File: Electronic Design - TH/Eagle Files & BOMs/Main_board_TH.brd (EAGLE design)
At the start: 90 x 137.2 mm, 41 parts, among them M1 ARDUINO-NANO-3.0, Q1 IRF9520, Q2 IRF9520

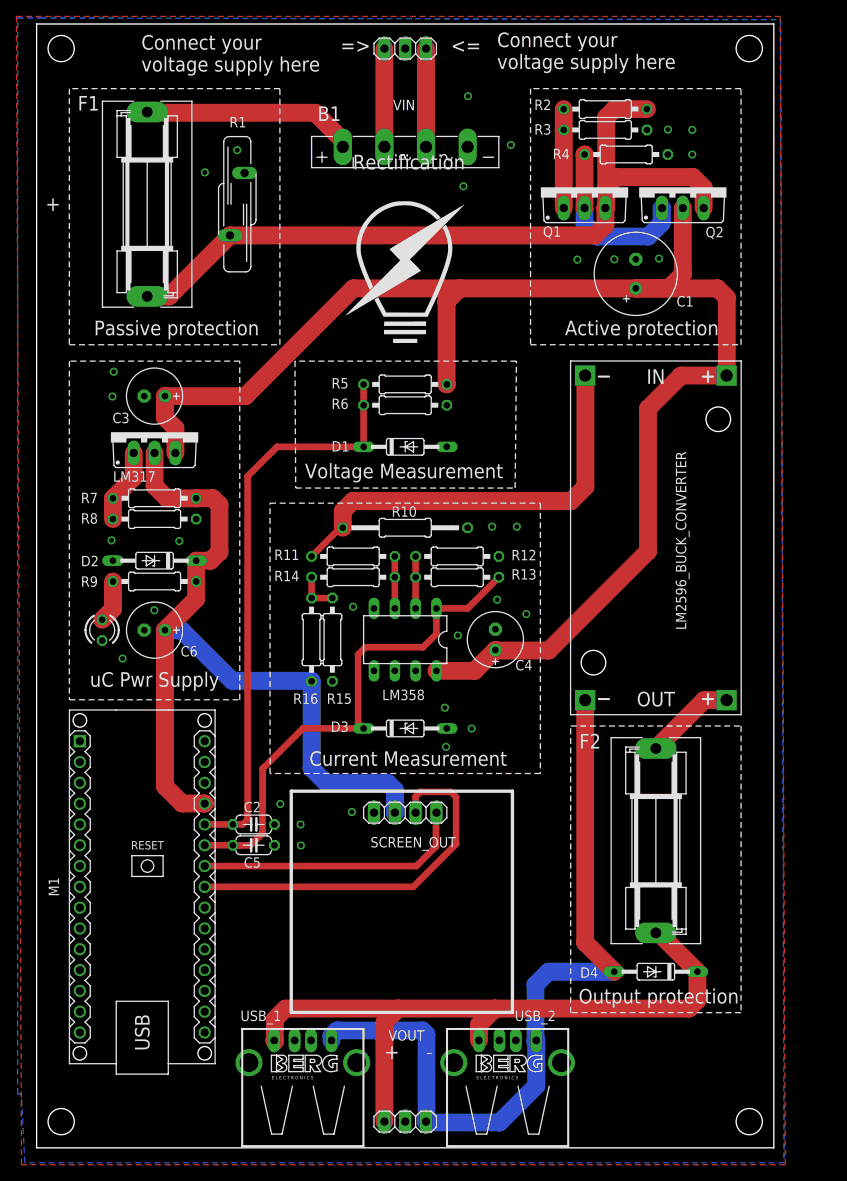
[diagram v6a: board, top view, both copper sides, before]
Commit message: Redoing names of sections so that they fit and adding in versioning and a place for people to put their names
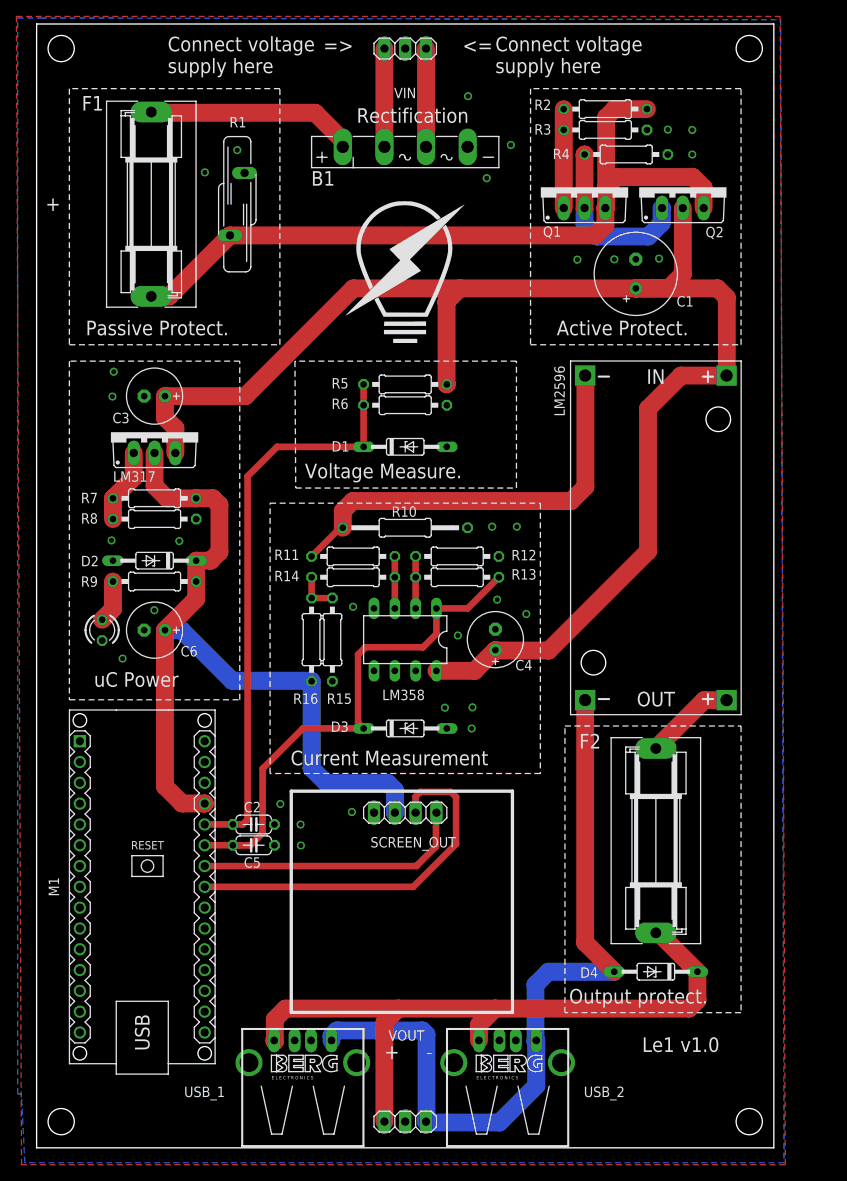
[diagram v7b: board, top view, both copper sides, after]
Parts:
- moved F1 0.50 mm to (14.0, 115.0)
- renumbered LM2596_BUCK_CONVERTER to LM2596
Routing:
- net VIN_UNPROTECTED: track 93.6 -> 93.1 mm
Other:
- board text added: "Active Protect."
- board text added: "Connect voltage supply here"
- board text added: "Le1 v1.0"
- board text added: "Output protect."
- board text added: "Passive Protect."
- board text added: "This Le1 belongs to:"
- board text added: "Voltage Measure."
- board text added: "uC Power"
- board text removed: "Active protection"
- board text removed: "Connect your voltage supply here"
- board text removed: "Output protection"
- board text removed: "Passive protection"
- board text removed: "Voltage Measurement"
- board text removed: "uC Pwr Supply"

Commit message: minor cosmetic changes in the silkscreen layer
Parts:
- moved D4 1.35 mm to (74.2, 21.3)
- moved F2 1.35 mm to (74.2, 37.3)
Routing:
- net VOUT_PREFUSE: track 11.1 -> 16.9 mm
- net VOUT_FINAL: track 85.1 -> 81.8 mm
- net N$10: track 96.1 -> 94.2 mm
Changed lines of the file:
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@@
 <wire x1="31.09" y1="16.34" x2="58.09" y2="16.34" width="0.4064" layer="21"/>
 <wire x1="58.09" y1="16.34" x2="58.09" y2="43.34" width="0.4064" layer="21"/>
-<text x="16" y="131" size="1.778" layer="25">Connect voltage
+<text x="34.5" y="135.5" size="1.778" layer="25" rot="R180">Connect voltage
 supply here </text>
 <wire x1="29.7" y1="129.11" x2="4" y2="129.11" width="0.15" layer="21" style="shortdash"/>
@@
 <wire x1="29.7" y1="97.84" x2="29.7" y2="129.11" width="0.15" layer="21" style="shortdash"/>
 <text x="52" y="133.5" size="1.778" layer="25">&lt;=</text>
-<text x="39.0672" y="124.9396" size="1.778" layer="25">Rectification</text>
-<text x="6" y="99" size="1.778" layer="25">Passive Protect.</text>
+<text x="37" y="124.9396" size="1.778" layer="25">Rectification</text>
+<text x="5.5" y="99" size="1.778" layer="25">Passive Protect.</text>
 <text x="63.5" y="99" size="1.778" layer="25">Active Protect.</text>
 <wire x1="61.5" y1="45.5" x2="28.5" y2="45.5" width="0.15" layer="21" style="shortdash"/>
@@
 <text x="32.75" y="81.54" size="1.778" layer="25">Voltage Measure.</text>
 <text x="31" y="46.5" size="1.778" layer="25">Current Measurement</text>
-<wire x1="86" y1="16.3" x2="64.5" y2="16.3" width="0.15" layer="21" style="shortdash"/>
-<wire x1="64.5" y1="16.3" x2="64.5" y2="51.3" width="0.15" layer="21" style="shortdash"/>
-<wire x1="64.5" y1="51.3" x2="86" y2="51.3" width="0.15" layer="21" style="shortdash"/>
+<wire x1="86" y1="16.3" x2="62.5" y2="16.3" width="0.15" layer="21" style="shortdash"/>
+<wire x1="62.5" y1="16.3" x2="62.5" y2="51.3" width="0.15" layer="21" style="shortdash"/>
+<wire x1="62.5" y1="51.3" x2="86" y2="51.3" width="0.15" layer="21" style="shortdash"/>
 <wire x1="86" y1="51.3" x2="86" y2="16.3" width="0.15" layer="21" style="shortdash"/>
-<text x="65" y="17.42" size="1.778" layer="25">Output protect.</text>
+<text x="64" y="17.42" size="1.778" layer="25">Output protect.</text>
 <text x="42.46" y="10.65" size="1.778" layer="25">+</text>
 <text x="47.54" y="10.65" size="1.778" layer="25">-</text>
@@
 <attribute name="VALUE" x="42.46" y="130.825" size="1.27" layer="27"/>
 </element>
-<element name="F2" library="fuse" package="SH22,5A" value="FUSESH22,5A" x="75.6" y="37.3" smashed="yes" rot="R270">
-<attribute name="MF" value="" x="75.6" y="37.3" size="1.778" layer="27" rot="R270" display="off"/>
-<attribute name="MPN" value="" x="75.6" y="37.3" size="1.778" layer="27" rot="R270" display="off"/>
-<attribute name="OC_NEWARK" value="unknown" x="75.6" y="37.3" size="1.778" layer="27" rot="R270" display="off"/>
-<attribute name="OC_FARNELL" value="unknown" x="75.6" y="37.3" size="1.778" layer="27" rot="R270" display="off"/>
-<attribute name="NAME" x="66.24" y="48.55" size="1.778" layer="25" ratio="10"/>
-<attribute name="VALUE" x="67.98" y="37.2746" size="1.778" layer="27" ratio="10" rot="R270"/>
+<element name="F2" library="fuse" package="SH22,5A" value="FUSESH22,5A" x="74.25" y="37.3" smashed="yes" rot="R270">
+<attribute name="MF" value="" x="74.25" y="37.3" size="1.778" layer="27" rot="R270" display="off"/>
+<attribute name="MPN" value="" x="74.25" y="37.3" size="1.778" layer="27" rot="R270" display="off"/>
+<attribute name="OC_NEWARK" value="unknown" x="74.25" y="37.3" size="1.778" layer="27" rot="R270" display="off"/>
+<attribute name="OC_FARNELL" value="unknown" x="74.25" y="37.3" size="1.778" layer="27" rot="R270" display="off"/>
+<attribute name="NAME" x="64.89" y="48.55" size="1.778" layer="25" ratio="10"/>
+<attribute name="VALUE" x="66.63" y="37.2746" size="1.778" layer="27" ratio="10" rot="R270"/>
 </element>
 <element name="D1" library="diode" package="DO35Z10" value="5.1V" x="45" y="85.38" smashed="yes">
@@
 <attribute name="VALUE" x="16.686" y="74.02" size="1.27" layer="27" ratio="10" rot="R180"/>
 </element>
-<element name="D4" library="diode" package="DO35Z10" value="5.1V" x="75.6" y="21.3" smashed="yes" rot="R180">
-<attribute name="NAME" x="68.556" y="21.83" size="1.27" layer="25" ratio="10" rot="R180"/>
-<attribute name="VALUE" x="77.886" y="23.84" size="1.27" layer="27" ratio="10" rot="R180"/>
+<element name="D4" library="diode" package="DO35Z10" value="5.1V" x="74.25" y="21.3" smashed="yes" rot="R180">
+<attribute name="NAME" x="67.206" y="21.83" size="1.27" layer="25" ratio="10" rot="R180"/>
+<attribute name="VALUE" x="76.536" y="23.84" size="1.27" layer="27" ratio="10" rot="R180"/>
 </element>
 <element name="UC_PWR" library="led" package="LED3MM" value="" x="8" y="63" smashed="yes" rot="R270">
@@
 </element>
 <element name="C4" library="resistor" package="E2,5-7" value="10u" x="56.01" y="61.84" smashed="yes" rot="R90">
-<attribute name="NAME" x="58.438" y="58.092" size="1.27" layer="25" ratio="10"/>
+<attribute name="NAME" x="58.7428" y="57.457" size="1.27" layer="25" ratio="10"/>
 <attribute name="VALUE" x="59.185" y="64.888" size="1.27" layer="27" ratio="10" rot="R90"/>
 </element>
@@
 <contactref element="F2" pad="2"/>
 <contactref element="VOUT" pad="1"/>
-<wire x1="75.6" y1="26.0478" x2="75.9322" y2="26.0478" width="2.1844" layer="1"/>
-<wire x1="75.9322" y1="26.0478" x2="80.68" y2="21.3" width="2.1844" layer="1"/>
 <contactref element="USB_1" pad="1"/>
 <contactref element="USB_2" pad="1"/>
-<wire x1="80.68" y1="21.3" x2="80.68" y2="17.84" width="2.1844" layer="1"/>
-<wire x1="80.68" y1="17.84" x2="79.64" y2="16.8" width="2.1844" layer="1"/>
-<wire x1="55.97" y1="16.8" x2="79.64" y2="16.8" width="2.1844" layer="1"/>
 <wire x1="44.17" y1="16.8" x2="55.97" y2="16.8" width="2.1844" layer="1"/>
 <wire x1="44.17" y1="16.8" x2="30.38" y2="16.8" width="2.1844" layer="1"/>
@@
 <wire x1="42.46" y1="3" x2="42.46" y2="15.09" width="2.1844" layer="1"/>
 <wire x1="42.46" y1="15.09" x2="44.17" y2="16.8" width="2.1844" layer="1"/>
+<wire x1="74.18" y1="16.8" x2="55.97" y2="16.8" width="2.1844" layer="1"/>
+<wire x1="74.25" y1="26.0478" x2="74.5822" y2="26.0478" width="2.1844" layer="1"/>
+<wire x1="74.5822" y1="26.0478" x2="79.33" y2="21.3" width="2.1844" layer="1"/>
+<wire x1="79.33" y1="21.3" x2="78.68" y2="21.3" width="2.1844" layer="1"/>
+<wire x1="78.68" y1="21.3" x2="74.18" y2="16.8" width="2.1844" layer="1"/>
 </signal>
 <signal name="VOUT_PREFUSE">
 <contactref element="F2" pad="1"/>
 <contactref element="LM2596" pad="OUT+"/>
-<wire x1="84.236" y1="54.458" x2="81.5058" y2="54.458" width="2.1844" layer="1"/>
-<wire x1="81.5058" y1="54.458" x2="75.6" y2="48.5522" width="2.1844" layer="1"/>
+<wire x1="84.236" y1="54.458" x2="84.236" y2="50.835" width="2.1844" layer="1"/>
+<wire x1="84.236" y1="50.835" x2="82.0166" y2="48.6156" width="2.1844" layer="1"/>
+<wire x1="82.0166" y1="48.6156" x2="73.0634" y2="48.6156" width="2.1844" layer="1"/>
+<wire x1="73.0634" y1="48.6156" x2="74.25" y2="48.5522" width="2.1844" layer="1"/>
 </signal>
 <signal name="GND1">
@@
 <contactref element="LM2596" pad="OUT-"/>
 <wire x1="66.964" y1="54.458" x2="66.964" y2="24.856" width="2.1844" layer="1"/>
-<wire x1="66.964" y1="24.856" x2="70.52" y2="21.3" width="2.1844" layer="1"/>
 <contactref element="USB_1" pad="4"/>
 <contactref element="USB_2" pad="4"/>
@@
 <wire x1="47.59" y1="13.65" x2="47.59" y2="3.05" width="2.1844" layer="16"/>
 <wire x1="47.54" y1="3" x2="47.59" y2="3.05" width="2.1844" layer="16"/>
-<wire x1="70.52" y1="21.3" x2="62.48" y2="21.3" width="2.1844" layer="16"/>
+<wire x1="69.17" y1="21.3" x2="62.48" y2="21.3" width="2.1844" layer="16"/>
 <wire x1="62.48" y1="21.3" x2="60.9" y2="19.72" width="2.1844" layer="16"/>
 <wire x1="60.9" y1="19.72" x2="60.9" y2="12.81" width="2.1844" layer="16"/>
@@
 <wire x1="56.52" y1="2.9" x2="47.64" y2="2.9" width="2.1844" layer="16"/>
 <wire x1="47.64" y1="2.9" x2="47.54" y2="3" width="2.1844" layer="16"/>
+<wire x1="66.9798" y1="24.8402" x2="66.964" y2="24.856" width="2.1844" layer="1"/>
+<wire x1="66.964" y1="24.856" x2="66.964" y2="23.506" width="2.1844" layer="1"/>
+<wire x1="66.964" y1="23.506" x2="69.17" y2="21.3" width="2.1844" layer="1"/>
 </signal>
 <signal name="A5">
